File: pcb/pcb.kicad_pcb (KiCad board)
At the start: 4 copper layers, 56 x 20.5 mm, 21 parts, among them J1 Conn_Coaxial, U1 XIAO-nRF52840-SMD, U2 NEO-M9V-20B, U3 AP2112K-3.3, U4 MCP73831-2-OT

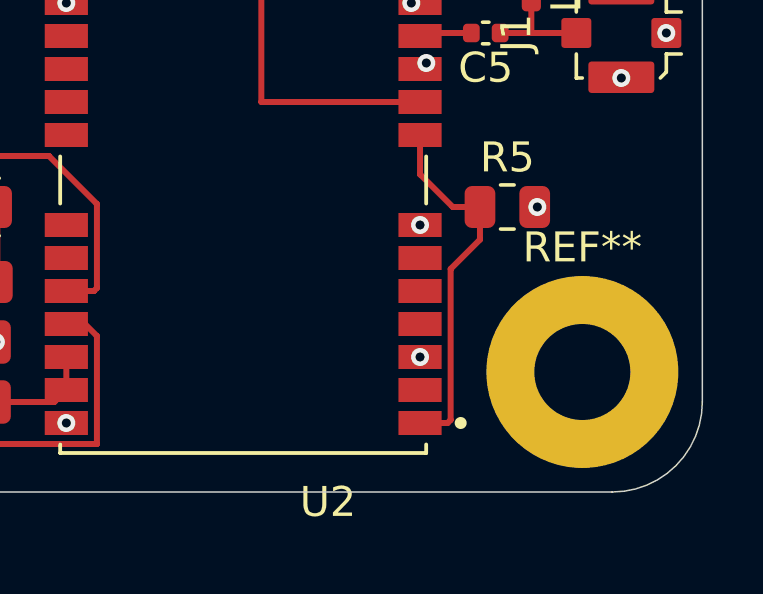
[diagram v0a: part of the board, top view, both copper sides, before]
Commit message: Update pcb from remove safeboot pull up
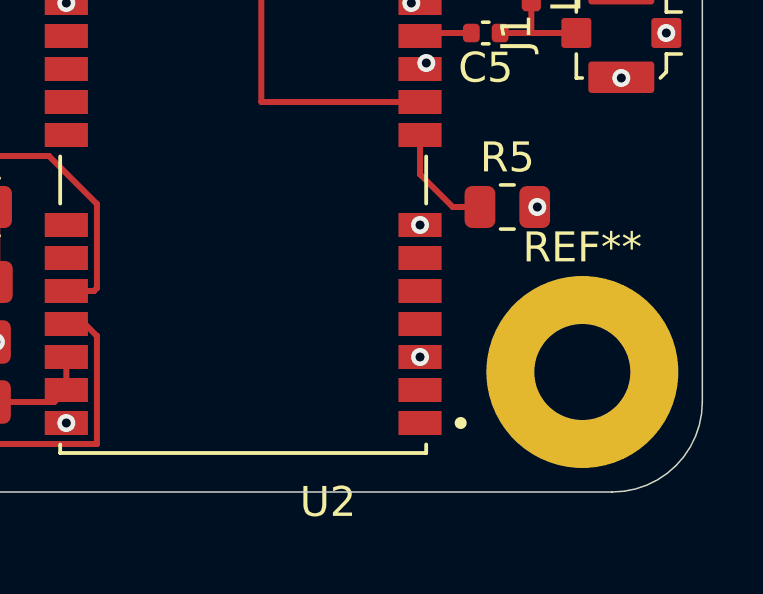
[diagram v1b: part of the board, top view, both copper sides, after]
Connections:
- U2 pad 1: Net-(U2-~{RESET}) -> unconnected-(U2-~{SAFEBOOT}-Pad1)
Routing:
- net Net-(U2-~{RESET}): track 12.3 -> 3.76 mm
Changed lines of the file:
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@@
 			)
 		)
-		(property "LCSC" "C88373"
+		(property "LCSC" "U.FL-R-SMT-1(10)"
 			(at 0 0 270)
 			(unlocked yes)
@@
 			)
 		)
-		(attr smd exclude_from_bom)
+		(attr smd)
 		(duplicate_pad_numbers_are_jumpers no)
 		(fp_line
@@
 			)
 		)
-		(property "LCSC" "C1779"
+		(property "LCSC" "CL21A475KAQNNNE"
 			(at 0 0 180)
 			(unlocked yes)
@@
 			)
 		)
-		(property "LCSC" "C34499"
+		(property "LCSC" "150080VS75000"
 			(at 0 0 0)
 			(unlocked yes)
@@
 			)
 		)
-		(property "LCSC" "C115488"
+		(property "LCSC" "LQG15HN27NJ02D"
 			(at 0 0 270)
 			(unlocked yes)
@@
 			)
 		)
-		(property "LCSC" "C114572"
+		(property "LCSC" "RC0805FR-072KL"
 			(at 0 0 180)
 			(unlocked yes)
@@
 			)
 		)
-		(property "LCSC" "C95781"
+		(property "LCSC" "RC0805FR-071KL"
 			(at 0 0 180)
 			(unlocked yes)
@@
 			)
 		)
-		(property "LCSC" "C76970"
+		(property "LCSC" "GRM1555C1H470JA01D"
 			(at 0 0 180)
 			(unlocked yes)
@@
 			)
 		)
-		(property "LCSC" "C49678"
+		(property "LCSC" "C0805C104K5RACTU"
 			(at 0 0 0)
 			(unlocked yes)
@@
 			)
 		)
-		(property "LCSC" "C162319"
+		(property "LCSC" "GRM21BC71C106KE11L"
 			(at 0 0 180)
 			(unlocked yes)
@@
 			)
 		)
-		(property "LCSC" "C424093"
+		(property "LCSC" "MCP73831T-2ACI/OT"
 			(at 0 0 270)
 			(unlocked yes)
@@
 			)
 		)
-		(attr through_hole exclude_from_bom dnp)
+		(attr through_hole dnp)
 		(duplicate_pad_numbers_are_jumpers no)
 		(fp_line
@@
 			)
 		)
-		(property "LCSC" "C1779"
+		(property "LCSC" "CL21A475KAQNNNE"
 			(at 0 0 180)
 			(unlocked yes)
@@
 			)
 		)
-		(property "LCSC" "C51118"
+		(property "LCSC" "AP2112K-3.3TRG1"
 			(at 0 0 90)
 			(unlocked yes)
@@
 			)
 		)
-		(property "LCSC" "C162319"
+		(property "LCSC" "GRM21BC71C106KE11L"
 			(at 0 0 0)
 			(unlocked yes)
@@
 			)
 		)
-		(property "LCSC" "C84376"
+		(property "LCSC" "RC0805FR-0710KL"
 			(at 0 0 270)
 			(unlocked yes)
@@
 			)
 		)
-		(attr smd exclude_from_bom dnp)
+		(attr smd dnp)
 		(duplicate_pad_numbers_are_jumpers no)
 		(fp_line
@@
 			(size 1.44 0.8)
 			(layers "F.Cu" "F.Mask" "F.Paste")
-			(net "Net-(U2-~{RESET})")
+			(net "unconnected-(U2-~{SAFEBOOT}-Pad1)")
 			(pinfunction "~{SAFEBOOT}_1")
-			(pintype "input")
+			(pintype "input+no_connect")
 			(solder_mask_margin 0.102)
 		)
@@
 			)
 		)
-		(property "LCSC" "C162319"
+		(property "LCSC" "GRM21BC71C106KE11L"
 			(at 0 0 90)
 			(unlocked yes)
@@
 			(at 0 1.65 0)
 			(layer "F.Fab")
+			(hide yes)
 			(effects
 				(font
@@
 			)
 		)
-		(property "LCSC" "C84376"
+		(property "LCSC" "RC0805FR-0710KL"
 			(at 0 0 0)
 			(unlocked yes)
@@
 			)
 		)
-		(attr exclude_from_bom dnp)
+		(attr dnp)
 		(duplicate_pad_numbers_are_jumpers no)
 		(fp_line
@@
 			)
 		)
-		(property "LCSC" "C84376"
+		(property "LCSC" "RC0805FR-0710KL"
 			(at 0 0 90)
 			(unlocked yes)
@@
 	)
 	(segment
-		(start 105.11 63.065)
-		(end 105.11 68.1)
-		(width 0.2)
-		(layer "F.Cu")
-		(net "Net-(U2-~{RESET})")
-	)
-	(segment
 		(start 105.18 61)
 		(end 104.09 59.91)
@@
 	)
 	(segment
-		(start 105.01 68.2)
-		(end 104.09 68.2)
-		(width 0.2)
-		(layer "F.Cu")
-		(net "Net-(U2-~{RESET})")
-	)
-	(segment
-		(start 106.0875 62.0875)
-		(end 106.0875 61)
-		(width 0.2)
-		(layer "F.Cu")
-		(net "Net-(U2-~{RESET})")
-	)
-	(segment
 		(start 104.09 59.91)
 		(end 104.09 59.915)
@@
 	)
 	(segment
-		(start 105.11 68.1)
-		(end 105.01 68.2)
-		(width 0.2)
-		(layer "F.Cu")
-		(net "Net-(U2-~{RESET})")
-	)
-	(segment
 		(start 104.09 58.6)
 		(end 104.09 59.91)
 		(width 0.2)
 		(layer "F.Cu")
-		(net "Net-(U2-~{RESET})")
-	)
-	(segment
-		(start 105.11 63.065)
-		(end 106.0875 62.0875)
-		(width 0.2)
-		(layer "F.Cu")
